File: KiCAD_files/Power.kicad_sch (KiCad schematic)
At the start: 44 parts, among them J101 Wago 6 contacts, P101 Power2, U101 AMC1311, U102 MCP6486UT-E/LT, U103 MCP6486UT-E/LT, U104 ACS723LLCTR-20AB

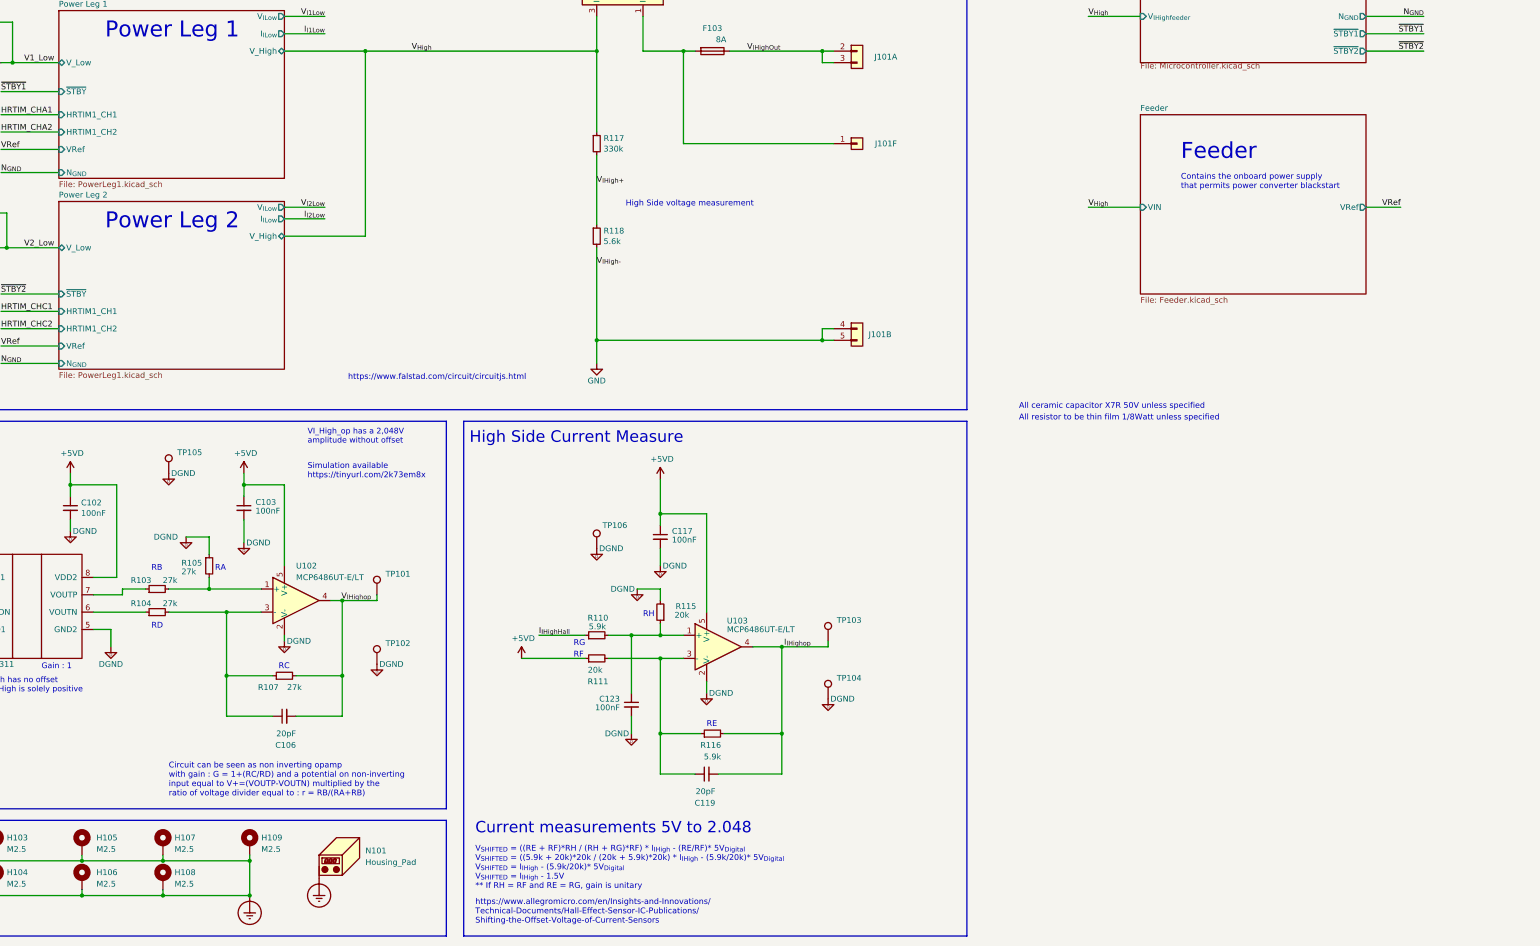
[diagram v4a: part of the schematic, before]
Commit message: more details on power signals generation from feeder and cleaned no pin to drive power pin error by addind power flag
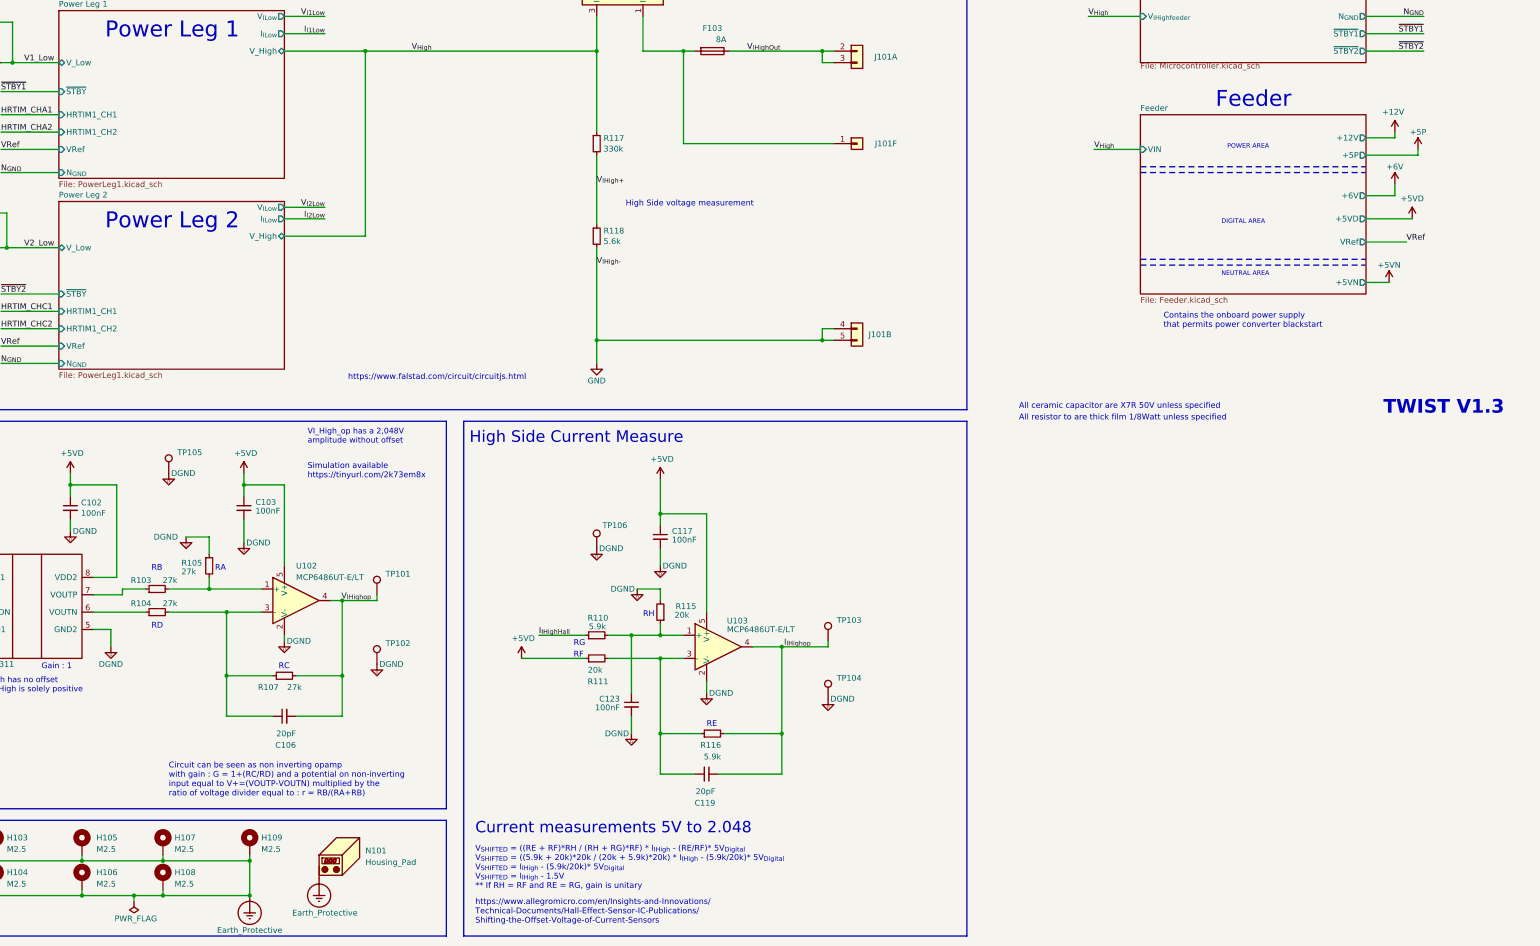
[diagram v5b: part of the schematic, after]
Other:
- sheet Feeder ports: added +12V, +5P, +5VD, +5VN, +6V; removed none
- note added: "All ceramic capacitor are X7R 50V unless specified"
- note added: "All resistor to are thick film 1/8Watt unless specified"
- note added: "DIGITAL AREA"
- note added: "NEUTRAL AREA"
- note added: "POWER AREA"
- note added: "TWIST V1.3"
- note removed: "All ceramic capacitor X7R 50V unless specified"
- note removed: "All resistor to be thin film 1/8Watt unless specified"

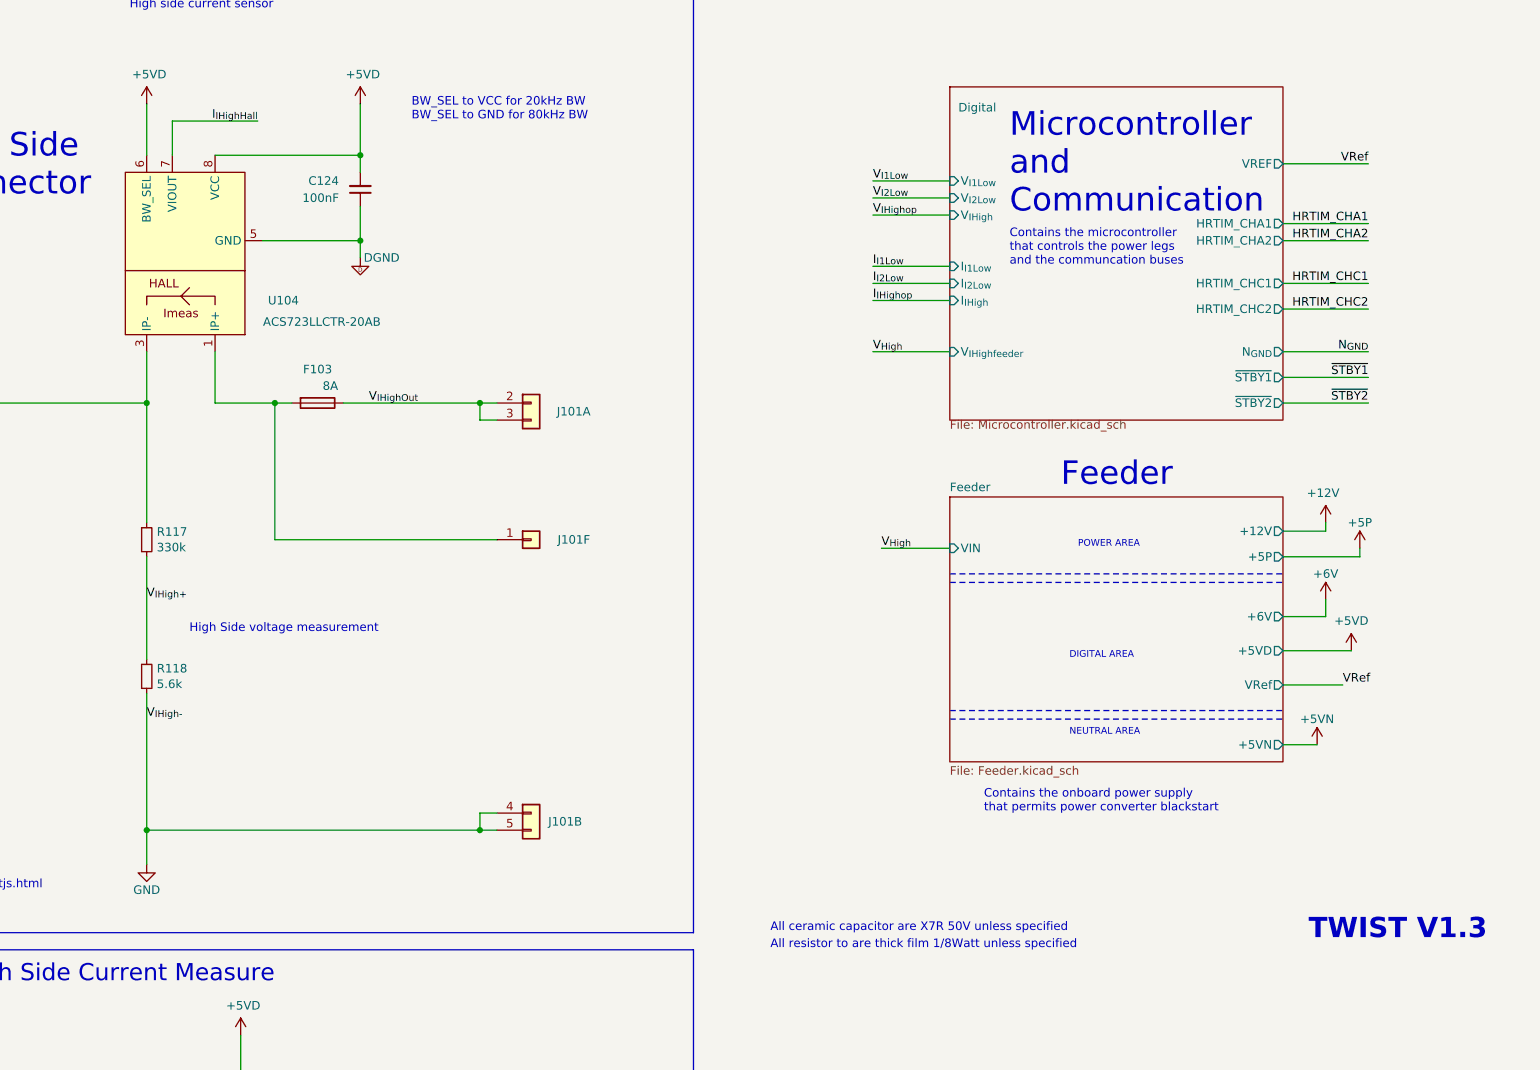
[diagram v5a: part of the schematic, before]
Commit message: New library power symbols and update template content
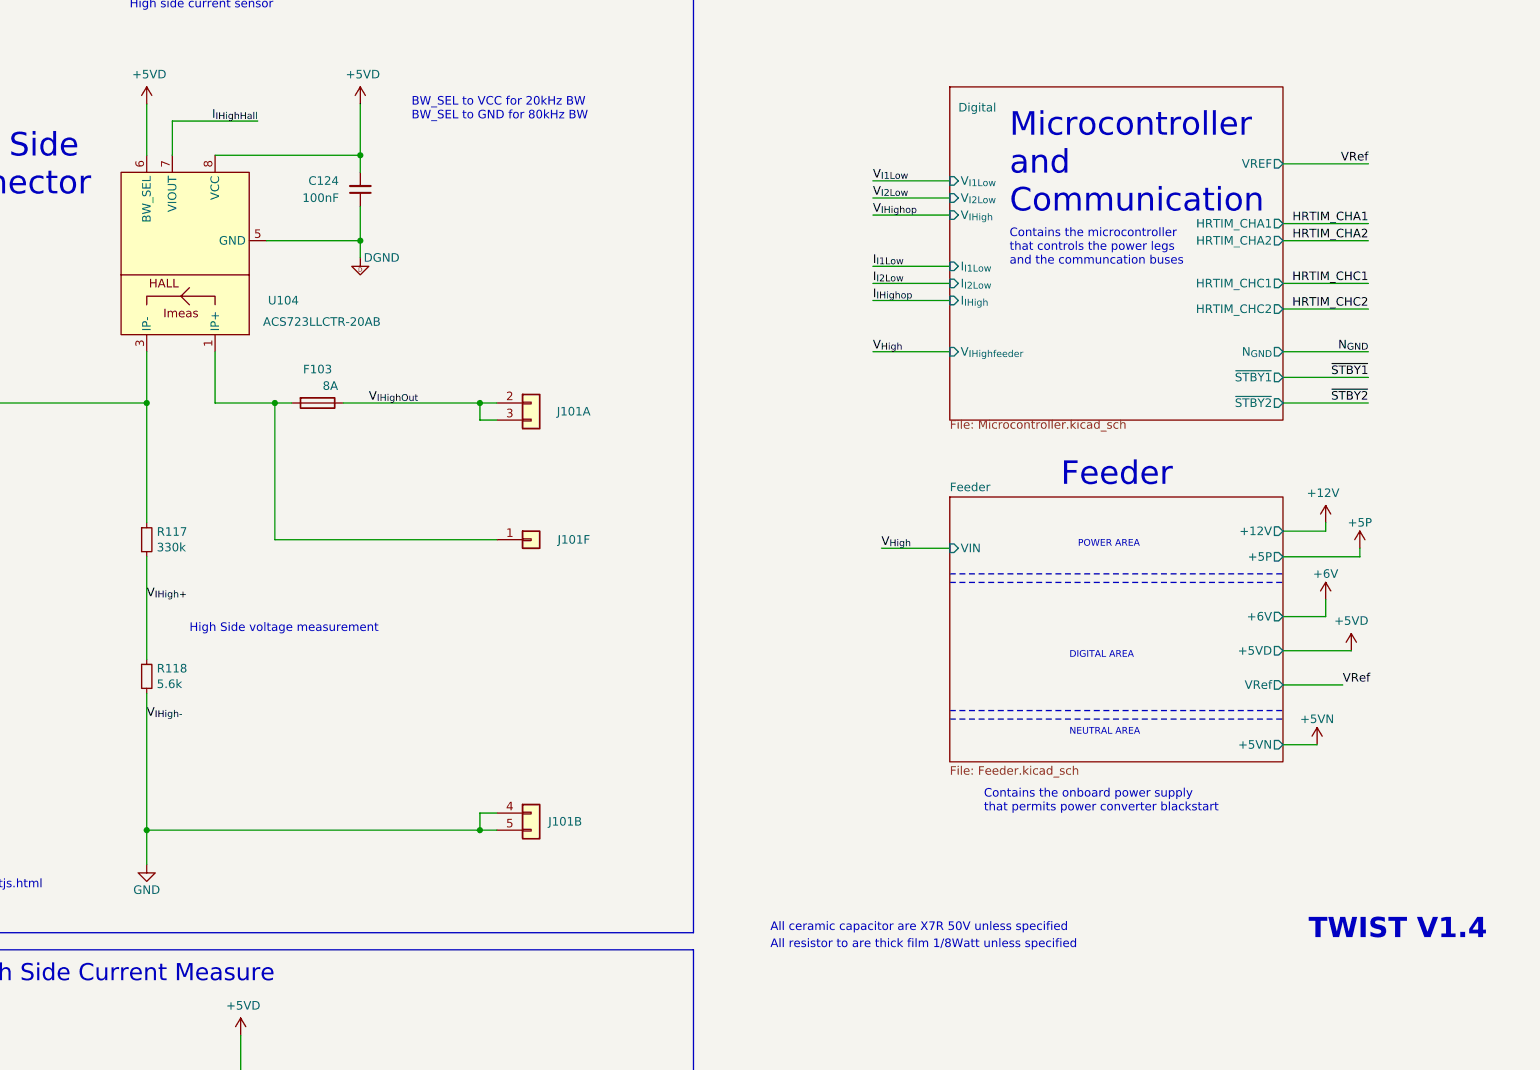
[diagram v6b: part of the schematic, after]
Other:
- note added: "TWIST V1.4"
- note removed: "TWIST V1.3"
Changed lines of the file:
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@@
   (junction (at 223.52 215.9) (diameter 0) (color 0 0 0 0)
   )
+  (junction (at 241.3 63.5) (diameter 0) (color 0 0 0 0)
+  )
   (junction (at 223.52 220.98) (diameter 0) (color 0 0 0 0)
   )
@@
   (junction (at 132.08 182.88) (diameter 0) (color 0 0 0 0)
   )
-  (junction (at 241.3 63.5) (diameter 0) (color 0 0 0 0)
-  )
   (junction (at 158.75 87.63) (diameter 0) (color 0 0 0 0)
   )
   (junction (at 96.52 273.05) (diameter 0) (color 0 0 0 0)
   )
+  (junction (at 77.47 273.05) (diameter 0) (color 0 0 0 0)
+  )
+  (junction (at 128.27 224.79) (diameter 0) (color 0 0 0 0)
+  )
+  (junction (at 223.52 237.49) (diameter 0) (color 0 0 0 0)
+  )
+  (junction (at 114.3 273.05) (diameter 0) (color 0 0 0 0)
+  )
+  (junction (at 241.3 50.8) (diameter 0) (color 0 0 0 0)
+  )
+  (junction (at 250.19 237.49) (diameter 0) (color 0 0 0 0)
+  )
+  (junction (at 259.08 151.13) (diameter 0) (color 0 0 0 0)
+  )
+  (junction (at 64.77 214.63) (diameter 0) (color 0 0 0 0)
+  )
+  (junction (at 133.35 273.05) (diameter 0) (color 0 0 0 0)
+  )
+  (junction (at 209.55 151.13) (diameter 0) (color 0 0 0 0)
+  )
+  (junction (at 217.17 215.9) (diameter 0) (color 0 0 0 0)
+  )
+  (junction (at 60.96 182.88) (diameter 0) (color 0 0 0 0)
+  )
+  (junction (at 81.28 90.17) (diameter 0) (color 0 0 0 0)
+  )
   (junction (at 209.55 87.63) (diameter 0) (color 0 0 0 0)
   )
-  (junction (at 77.47 273.05) (diameter 0) (color 0 0 0 0)
-  )
-  (junction (at 128.27 224.79) (diameter 0) (color 0 0 0 0)
-  )
-  (junction (at 223.52 237.49) (diameter 0) (color 0 0 0 0)
-  )
-  (junction (at 114.3 273.05) (diameter 0) (color 0 0 0 0)
-  )
-  (junction (at 241.3 50.8) (diameter 0) (color 0 0 0 0)
-  )
-  (junction (at 250.19 237.49) (diameter 0) (color 0 0 0 0)
-  )
-  (junction (at 259.08 151.13) (diameter 0) (color 0 0 0 0)
-  )
-  (junction (at 64.77 214.63) (diameter 0) (color 0 0 0 0)
-  )
-  (junction (at 133.35 273.05) (diameter 0) (color 0 0 0 0)
-  )
-  (junction (at 209.55 151.13) (diameter 0) (color 0 0 0 0)
-  )
-  (junction (at 217.17 215.9) (diameter 0) (color 0 0 0 0)
-  )
-  (junction (at 60.96 182.88) (diameter 0) (color 0 0 0 0)
-  )
-  (junction (at 81.28 90.17) (diameter 0) (color 0 0 0 0)
-  )
   (junction (at 153.67 224.79) (diameter 0) (color 0 0 0 0)
   )
@@
     (stroke (width 0) (type default))
   )
+  (wire (pts (xy 213.36 45.72) (xy 213.36 50.8))
+    (stroke (width 0) (type default))
+  )
   (wire (pts (xy 228.6 87.63) (xy 231.14 87.63))
     (stroke (width 0.35) (type default))
@@
     (stroke (width 0) (type default))
   )
+  (wire (pts (xy 227.33 63.5) (xy 241.3 63.5))
+    (stroke (width 0) (type default))
+  )
   (wire (pts (xy 93.98 182.88) (xy 104.14 182.88))
     (stroke (width 0) (type default))
@@
     (stroke (width 0) (type default))
   )
+  (wire (pts (xy 241.3 63.5) (xy 241.3 66.04))
+    (stroke (width 0) (type default))
+  )
   (wire (pts (xy 69.85 210.82) (xy 69.85 214.63))
     (stroke (width 0) (type default))
@@
   )
   (wire (pts (xy 110.49 205.74) (xy 105.41 205.74))
-    (stroke (width 0) (type default))
-  )
-  (wire (pts (xy 226.695 63.5) (xy 241.3 63.5))
     (stroke (width 0) (type default))
   )
@@
     (stroke (width 0) (type default))
   )
-  (wire (pts (xy 241.3 63.5) (xy 241.3 66.04))
-    (stroke (width 0) (type default))
-  )
   (wire (pts (xy 193.04 220.98) (xy 207.01 220.98))
     (stroke (width 0) (type default))
@@
   )
   (wire (pts (xy 107.95 273.05) (xy 114.3 273.05))
-    (stroke (width 0) (type default))
-  )
-  (wire (pts (xy 213.36 50.8) (xy 213.36 45.72))
     (stroke (width 0) (type default))
   )
@@
     (effects (font (size 1.27 1.27)) (justify left bottom))
   )
-  (text "TWIST V1.3" (at 382.27 167.64 0)
+  (text "TWIST V1.4" (at 382.27 167.64 0)
     (effects (font (size 3 3) (thickness 0.6) bold) (justify left bottom))
   )

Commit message: Renamed power supply names for better schematic understanding
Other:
- sheet Digital ports: added N_{PGND}; removed N_{GND}
- sheet Feeder ports: added +12V_PGND, +5V_DGND, +5V_NEUTRAL, +5V_PGND, +6V_DGND; removed +12V, +5P, +5VD, +5VN, +6V
- sheet Power Leg 1 ports: added N_{PGND}; removed N_{GND}
- sheet Power Leg 2 ports: added N_{PGND}; removed N_{GND}
- note added: "BW_SEL to VCC for 20kHz BW BW_SEL to PGND for 80kHz BW"
- note removed: "BW_SEL to VCC for 20kHz BW BW_SEL to GND for 80kHz BW"
- moved on the sheet: C101, C102, C106, F102, J101E, J101H, R103, R104, R105, R107, TP101, TP102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
